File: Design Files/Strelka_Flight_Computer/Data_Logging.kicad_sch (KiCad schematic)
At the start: 2 parts

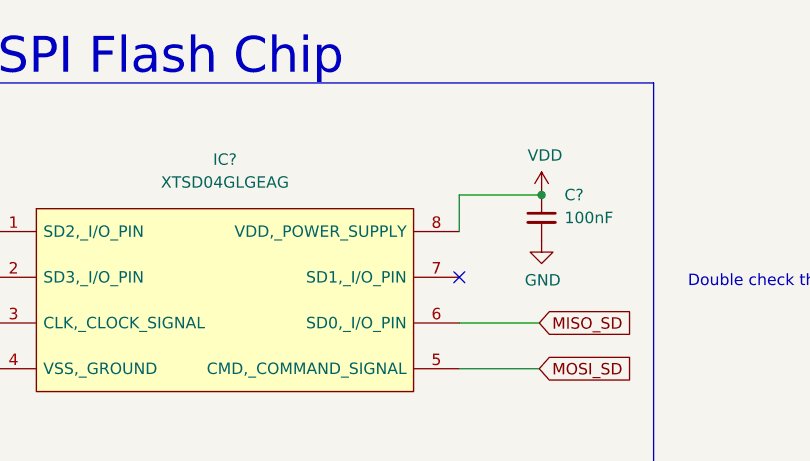
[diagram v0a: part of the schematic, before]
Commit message: Working SPICE sim for ematch continuity circuit
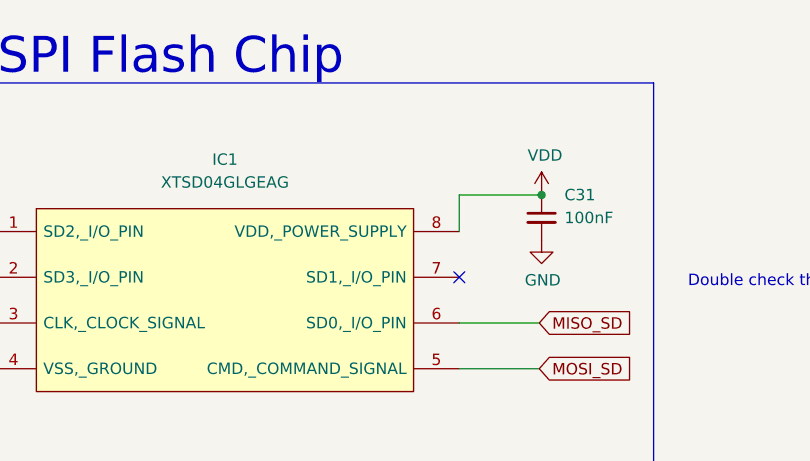
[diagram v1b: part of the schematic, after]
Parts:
- gave numbers to parts that had none: 2
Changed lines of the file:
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@@
   (symbol (lib_id "Device:C_Small") (at 106.299 41.656 0) (unit 1)
     (in_bom yes) (on_board yes)
-    (property "Reference" "C?" (id 0) (at 108.839 39.116 0)
+    (property "Reference" "C31" (id 0) (at 108.839 39.116 0)
       (effects (font (size 1.27 1.27)) (justify left))
     )
@@
   (symbol (lib_id "XTSD04GLGEAG:XTSD04GLGEAG") (at 45.085 50.8 0) (unit 1)
     (in_bom yes) (on_board yes) (fields_autoplaced)
-    (property "Reference" "IC?" (id 0) (at 71.12 35.179 0))
+    (property "Reference" "IC1" (id 0) (at 71.12 35.179 0))
     (property "Value" "XTSD04GLGEAG" (id 1) (at 71.12 37.719 0))
     (property "Footprint" "SON127P800X600X95-8N" (id 2) (at 104.775 48.26 0)
@@
   (symbol (lib_id "power:VDD") (at 106.299 39.116 0) (unit 1)
     (in_bom yes) (on_board yes)
-    (property "Reference" "#PWR?" (id 0) (at 106.299 42.926 0)
+    (property "Reference" "#PWR0194" (id 0) (at 106.299 42.926 0)
       (effects (font (size 1.27 1.27)) hide)
     )
@@
   (symbol (lib_id "power:GND") (at 106.299 44.196 0) (unit 1)
     (in_bom yes) (on_board yes)
-    (property "Reference" "#PWR?" (id 0) (at 106.299 50.546 0)
+    (property "Reference" "#PWR0195" (id 0) (at 106.299 50.546 0)
       (effects (font (size 1.27 1.27)) hide)
     )
@@
   (symbol (lib_id "power:GND") (at 41.275 60.96 0) (unit 1)
     (in_bom yes) (on_board yes)
-    (property "Reference" "#PWR?" (id 0) (at 41.275 67.31 0)
+    (property "Reference" "#PWR0196" (id 0) (at 41.275 67.31 0)
       (effects (font (size 1.27 1.27)) hide)
     )

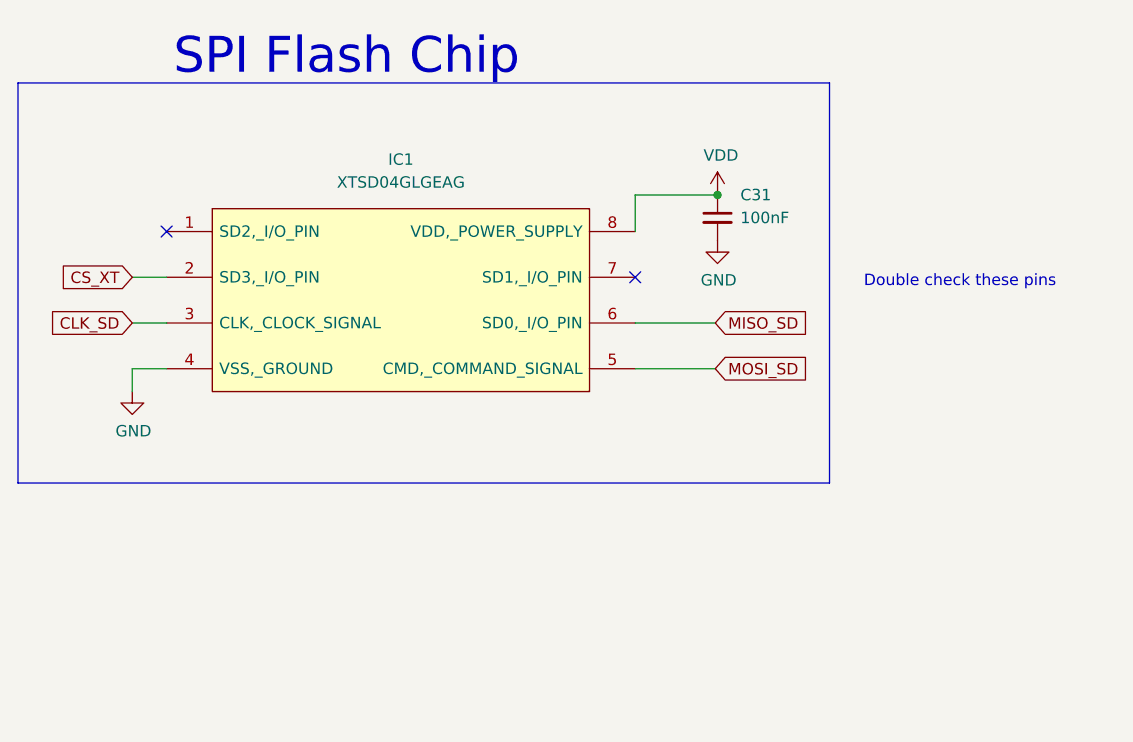
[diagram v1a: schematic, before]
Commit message: Added power board, almost finished Strelka schematic
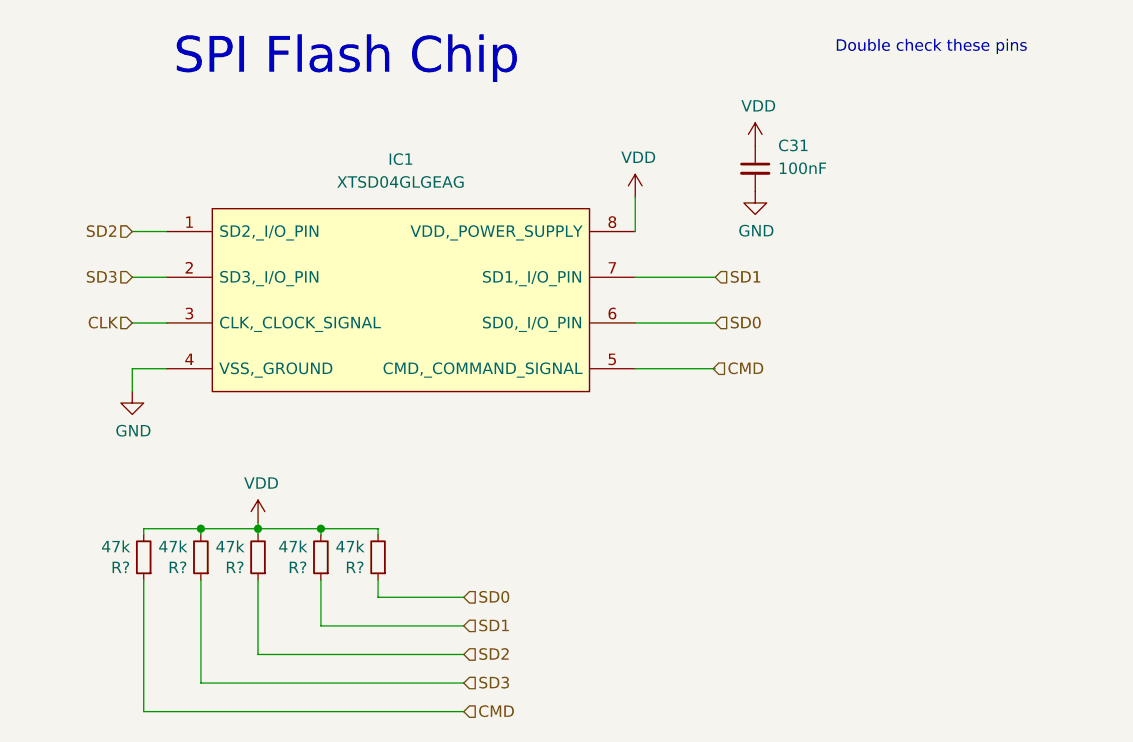
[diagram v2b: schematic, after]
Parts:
- added R? (x5): 47k, Resistor_SMD:R_0603_1608Metric_Pad0.98x0.95mm_HandSolder, symbol Nebula-rescue:R_Small-Device-H7_FlightComputer-rescue
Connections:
- net VDD: now also R?.2, R?.2, R?.2, R?.2, R?.2
- net SD2: now reaches IC1.1 (SD2,_I/O_PIN)
- net SD2: now also R?.1
- net SD1: now reaches IC1.7 (SD1,_I/O_PIN)
- net SD1: now also R?.1
- net CLK_SD renamed CLK
- net CS_XT renamed SD3
- net SD3: now also R?.1
- net MISO_SD renamed SD0
- net SD0: now also R?.1
- net MOSI_SD renamed CMD
- net CMD: now also R?.1
- no-connect marks 2 -> 0
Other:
- moved on the sheet: C31

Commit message: Added new UBLOX GPS
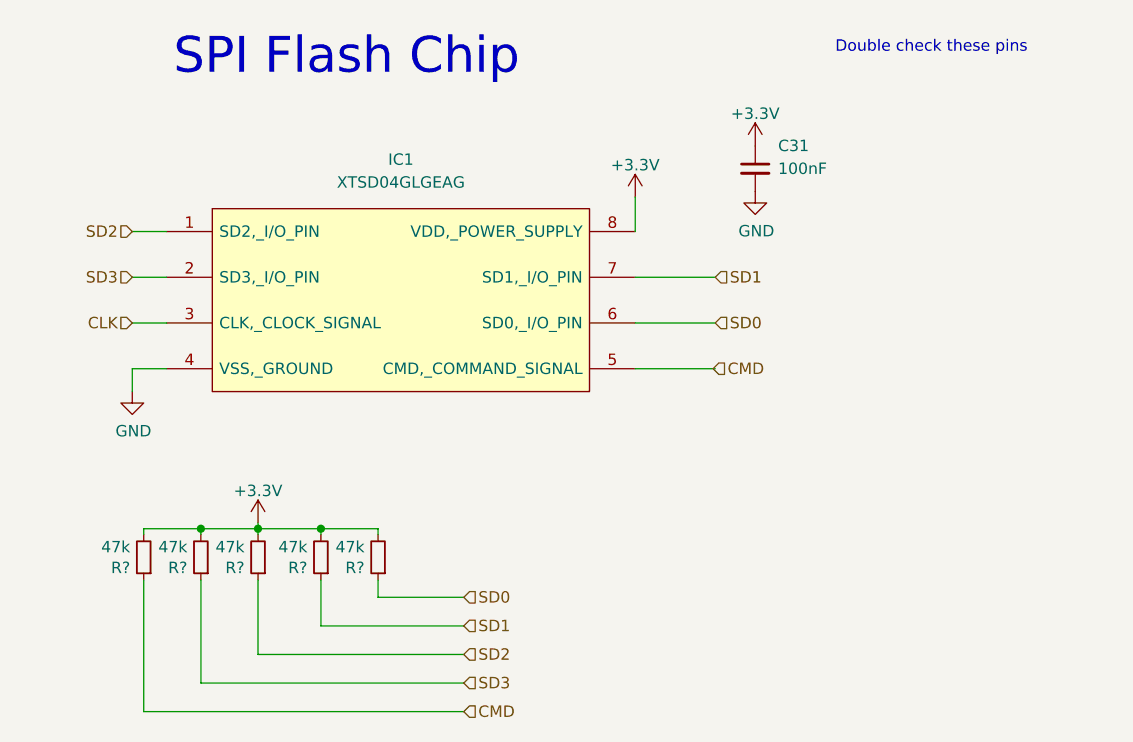
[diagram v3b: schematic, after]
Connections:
- net VDD renamed +3V3
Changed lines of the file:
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@@
     (pin "2")
   )
-  (symbol (lib_id "power:VDD") (at 97.155 39.37 0) (unit 1)
-    (in_bom yes) (on_board yes)
-    (property "Reference" "#PWR?" (id 0) (at 97.155 43.18 0)
+  (symbol (lib_id "power:+3.3V") (at 110.49 33.655 0) (unit 1)
+    (in_bom yes) (on_board yes) (fields_autoplaced)
+    (property "Reference" "#PWR?" (id 0) (at 110.49 37.465 0)
       (effects (font (size 1.27 1.27)) hide)
     )
-    (property "Value" "VDD" (id 1) (at 97.536 34.9758 0))
-    (property "Footprint" "" (id 2) (at 97.155 39.37 0)
+    (property "Value" "+3.3V" (id 1) (at 110.49 30.0792 0))
+    (property "Footprint" "" (id 2) (at 110.49 33.655 0)
       (effects (font (size 1.27 1.27)) hide)
     )
-    (property "Datasheet" "" (id 3) (at 97.155 39.37 0)
-      (effects (font (size 1.27 1.27)) hide)
-    )
-    (pin "1")
-  )
-  (symbol (lib_id "power:VDD") (at 55.245 75.565 0) (unit 1)
-    (in_bom yes) (on_board yes)
-    (property "Reference" "#PWR?" (id 0) (at 55.245 79.375 0)
-      (effects (font (size 1.27 1.27)) hide)
-    )
-    (property "Value" "VDD" (id 1) (at 55.626 71.1708 0))
-    (property "Footprint" "" (id 2) (at 55.245 75.565 0)
-      (effects (font (size 1.27 1.27)) hide)
-    )
-    (property "Datasheet" "" (id 3) (at 55.245 75.565 0)
+    (property "Datasheet" "" (id 3) (at 110.49 33.655 0)
       (effects (font (size 1.27 1.27)) hide)
     )
@@
     (pin "8")
   )
-  (symbol (lib_id "power:VDD") (at 110.49 33.655 0) (unit 1)
-    (in_bom yes) (on_board yes)
-    (property "Reference" "#PWR0194" (id 0) (at 110.49 37.465 0)
+  (symbol (lib_id "power:+3.3V") (at 97.155 39.37 0) (unit 1)
+    (in_bom yes) (on_board yes) (fields_autoplaced)
+    (property "Reference" "#PWR?" (id 0) (at 97.155 43.18 0)
       (effects (font (size 1.27 1.27)) hide)
     )
-    (property "Value" "VDD" (id 1) (at 110.871 29.2608 0))
-    (property "Footprint" "" (id 2) (at 110.49 33.655 0)
+    (property "Value" "+3.3V" (id 1) (at 97.155 35.7942 0))
+    (property "Footprint" "" (id 2) (at 97.155 39.37 0)
       (effects (font (size 1.27 1.27)) hide)
     )
-    (property "Datasheet" "" (id 3) (at 110.49 33.655 0)
+    (property "Datasheet" "" (id 3) (at 97.155 39.37 0)
       (effects (font (size 1.27 1.27)) hide)
     )
@@
       (effects (font (size 1.27 1.27)) hide)
     )
+    (pin "1")
+  )
+  (symbol (lib_id "power:+3.3V") (at 55.245 75.565 0) (unit 1)
+    (in_bom yes) (on_board yes) (fields_autoplaced)
+    (property "Reference" "#PWR?" (id 0) (at 55.245 79.375 0)
+      (effects (font (size 1.27 1.27)) hide)
+    )
+    (property "Value" "+3.3V" (id 1) (at 55.245 71.9892 0))
+    (property "Footprint" "" (id 2) (at 55.245 75.565 0)
+      (effects (font (size 1.27 1.27)) hide)
+    )
+    (property "Datasheet" "" (id 3) (at 55.245 75.565 0)
+      (effects (font (size 1.27 1.27)) hide)
+    )

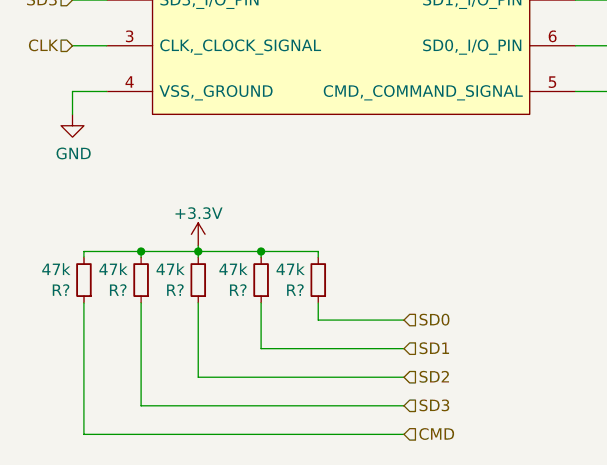
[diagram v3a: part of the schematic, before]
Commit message: Added motor driver to power board
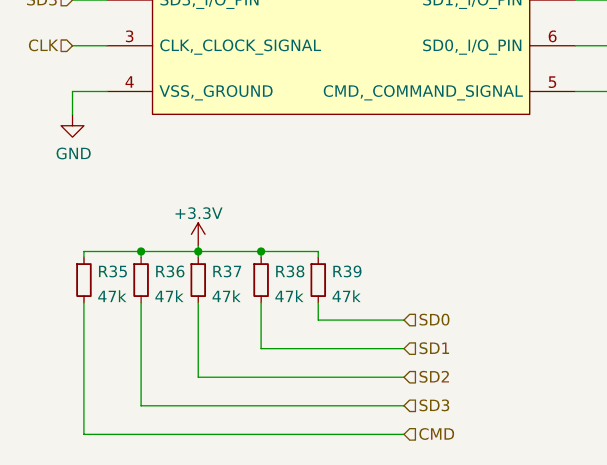
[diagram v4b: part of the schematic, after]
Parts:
- removed R? (x5): 47k, Resistor_SMD:R_0603_1608Metric_Pad0.98x0.95mm_HandSolder, symbol Nebula-rescue:R_Small-Device-H7_FlightComputer-rescue
- added R35, R36, R37, R38, R39: 47k, Resistor_SMD:R_0603_1608Metric, symbol Device:R_Small
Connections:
- net +3V3: now also R35.1, R36.1, R37.1, R38.1, R39.1
- net CMD: now also R35.2
- net SD0: now also R39.2
- net SD1: now also R38.2
- net SD2: now also R37.2
- net SD3: now also R36.2
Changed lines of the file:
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@@
     (effects (font (size 1.27 1.27)) (justify right))
   )
-  (symbol (lib_id "Nebula-rescue:R_Small-Device-H7_FlightComputer-rescue") (at 62.23 79.375 180) (unit 1)
-    (in_bom yes) (on_board yes)
-    (property "Reference" "R?" (id 0) (at 60.7314 80.5434 0)
-      (effects (font (size 1.27 1.27)) (justify left))
-    )
-    (property "Value" "47k" (id 1) (at 60.7314 78.232 0)
-      (effects (font (size 1.27 1.27)) (justify left))
-    )
-    (property "Footprint" "Resistor_SMD:R_0603_1608Metric_Pad0.98x0.95mm_HandSolder" (id 2) (at 62.23 79.375 0)
-      (effects (font (size 1.27 1.27)) hide)
-    )
-    (property "Datasheet" "~" (id 3) (at 62.23 79.375 0)
-      (effects (font (size 1.27 1.27)) hide)
-    )
-    (pin "1")
-    (pin "2")
-  )
   (symbol (lib_id "power:+3.3V") (at 110.49 33.655 0) (unit 1)
     (in_bom yes) (on_board yes) (fields_autoplaced)
-    (property "Reference" "#PWR?" (id 0) (at 110.49 37.465 0)
+    (property "Reference" "#PWR0171" (id 0) (at 110.49 37.465 0)
       (effects (font (size 1.27 1.27)) hide)
     )
@@
     )
     (pin "1")
+  )
+  (symbol (lib_id "Device:R_Small") (at 62.23 79.375 0) (unit 1)
+    (in_bom yes) (on_board yes) (fields_autoplaced)
+    (property "Reference" "R38" (id 0) (at 63.7287 78.4665 0)
+      (effects (font (size 1.27 1.27)) (justify left))
+    )
+    (property "Value" "47k" (id 1) (at 63.7287 81.2416 0)
+      (effects (font (size 1.27 1.27)) (justify left))
+    )
+    (property "Footprint" "Resistor_SMD:R_0603_1608Metric" (id 2) (at 62.23 79.375 0)
+      (effects (font (size 1.27 1.27)) hide)
+    )
+    (property "Datasheet" "~" (id 3) (at 62.23 79.375 0)
+      (effects (font (size 1.27 1.27)) hide)
+    )
+    (pin "1")
+    (pin "2")
   )
   (symbol (lib_id "Device:C_Small") (at 110.49 36.195 0) (unit 1)
@@
     (pin "8")
   )
+  (symbol (lib_id "Device:R_Small") (at 42.545 79.375 0) (unit 1)
+    (in_bom yes) (on_board yes) (fields_autoplaced)
+    (property "Reference" "R35" (id 0) (at 44.0437 78.4665 0)
+      (effects (font (size 1.27 1.27)) (justify left))
+    )
+    (property "Value" "47k" (id 1) (at 44.0437 81.2416 0)
+      (effects (font (size 1.27 1.27)) (justify left))
+    )
+    (property "Footprint" "Resistor_SMD:R_0603_1608Metric" (id 2) (at 42.545 79.375 0)
+      (effects (font (size 1.27 1.27)) hide)
+    )
+    (property "Datasheet" "~" (id 3) (at 42.545 79.375 0)
+      (effects (font (size 1.27 1.27)) hide)
+    )
+    (pin "1")
+    (pin "2")
+  )
   (symbol (lib_id "power:+3.3V") (at 97.155 39.37 0) (unit 1)
     (in_bom yes) (on_board yes) (fields_autoplaced)
-    (property "Reference" "#PWR?" (id 0) (at 97.155 43.18 0)
+    (property "Reference" "#PWR0170" (id 0) (at 97.155 43.18 0)
       (effects (font (size 1.27 1.27)) hide)
     )
@@
     (pin "1")
   )
-  (symbol (lib_id "Nebula-rescue:R_Small-Device-H7_FlightComputer-rescue") (at 55.245 79.375 180) (unit 1)
-    (in_bom yes) (on_board yes)
-    (property "Reference" "R?" (id 0) (at 53.7464 80.5434 0)
-      (effects (font (size 1.27 1.27)) (justify left))
-    )
-    (property "Value" "47k" (id 1) (at 53.7464 78.232 0)
-      (effects (font (size 1.27 1.27)) (justify left))
-    )
-    (property "Footprint" "Resistor_SMD:R_0603_1608Metric_Pad0.98x0.95mm_HandSolder" (id 2) (at 55.245 79.375 0)
+  (symbol (lib_id "Device:R_Small") (at 55.245 79.375 0) (unit 1)
+    (in_bom yes) (on_board yes) (fields_autoplaced)
+    (property "Reference" "R37" (id 0) (at 56.7437 78.4665 0)
+      (effects (font (size 1.27 1.27)) (justify left))
+    )
+    (property "Value" "47k" (id 1) (at 56.7437 81.2416 0)
+      (effects (font (size 1.27 1.27)) (justify left))
+    )
+    (property "Footprint" "Resistor_SMD:R_0603_1608Metric" (id 2) (at 55.245 79.375 0)
       (effects (font (size 1.27 1.27)) hide)
     )
@@
     (pin "2")
   )
-  (symbol (lib_id "Nebula-rescue:R_Small-Device-H7_FlightComputer-rescue") (at 48.895 79.375 180) (unit 1)
-    (in_bom yes) (on_board yes)
-    (property "Reference" "R?" (id 0) (at 47.3964 80.5434 0)
-      (effects (font (size 1.27 1.27)) (justify left))
-    )
-    (property "Value" "47k" (id 1) (at 47.3964 78.232 0)
-      (effects (font (size 1.27 1.27)) (justify left))
-    )
-    (property "Footprint" "Resistor_SMD:R_0603_1608Metric_Pad0.98x0.95mm_HandSolder" (id 2) (at 48.895 79.375 0)
+  (symbol (lib_id "Device:R_Small") (at 48.895 79.375 0) (unit 1)
+    (in_bom yes) (on_board yes) (fields_autoplaced)
+    (property "Reference" "R36" (id 0) (at 50.3937 78.4665 0)
+      (effects (font (size 1.27 1.27)) (justify left))
+    )
+    (property "Value" "47k" (id 1) (at 50.3937 81.2416 0)
+      (effects (font (size 1.27 1.27)) (justify left))
+    )
+    (property "Footprint" "Resistor_SMD:R_0603_1608Metric" (id 2) (at 48.895 79.375 0)
       (effects (font (size 1.27 1.27)) hide)
     )
     (property "Datasheet" "~" (id 3) (at 48.895 79.375 0)
+      (effects (font (size 1.27 1.27)) hide)
+    )
+    (pin "1")
+    (pin "2")
+  )
+  (symbol (lib_id "Device:R_Small") (at 68.58 79.375 0) (unit 1)
+    (in_bom yes) (on_board yes) (fields_autoplaced)
+    (property "Reference" "R39" (id 0) (at 70.0787 78.4665 0)
+      (effects (font (size 1.27 1.27)) (justify left))
+    )
+    (property "Value" "47k" (id 1) (at 70.0787 81.2416 0)
+      (effects (font (size 1.27 1.27)) (justify left))
+    )
+    (property "Footprint" "Resistor_SMD:R_0603_1608Metric" (id 2) (at 68.58 79.375 0)
+      (effects (font (size 1.27 1.27)) hide)
+    )
+    (property "Datasheet" "~" (id 3) (at 68.58 79.375 0)
       (effects (font (size 1.27 1.27)) hide)
     )
@@
     (pin "1")
   )
-  (symbol (lib_id "Nebula-rescue:R_Small-Device-H7_FlightComputer-rescue") (at 68.58 79.375 180) (unit 1)
-    (in_bom yes) (on_board yes)
-    (property "Reference" "R?" (id 0) (at 67.0814 80.5434 0)
-      (effects (font (size 1.27 1.27)) (justify left))
-    )
-    (property "Value" "47k" (id 1) (at 67.0814 78.232 0)
-      (effects (font (size 1.27 1.27)) (justify left))
-    )
-    (property "Footprint" "Resistor_SMD:R_0603_1608Metric_Pad0.98x0.95mm_HandSolder" (id 2) (at 68.58 79.375 0)
-      (effects (font (size 1.27 1.27)) hide)
-    )
-    (property "Datasheet" "~" (id 3) (at 68.58 79.375 0)
-      (effects (font (size 1.27 1.27)) hide)
-    )
-    (pin "1")
-    (pin "2")
-  )
-  (symbol (lib_id "Nebula-rescue:R_Small-Device-H7_FlightComputer-rescue") (at 42.545 79.375 180) (unit 1)
-    (in_bom yes) (on_board yes)
-    (property "Reference" "R?" (id 0) (at 41.0464 80.5434 0)
-      (effects (font (size 1.27 1.27)) (justify left))
-    )
-    (property "Value" "47k" (id 1) (at 41.0464 78.232 0)
-      (effects (font (size 1.27 1.27)) (justify left))
-    )
-    (property "Footprint" "Resistor_SMD:R_0603_1608Metric_Pad0.98x0.95mm_HandSolder" (id 2) (at 42.545 79.375 0)
-      (effects (font (size 1.27 1.27)) hide)
-    )
-    (property "Datasheet" "~" (id 3) (at 42.545 79.375 0)
-      (effects (font (size 1.27 1.27)) hide)
-    )
-    (pin "1")
-    (pin "2")
-  )
   (symbol (lib_id "power:GND") (at 41.275 60.96 0) (unit 1)
     (in_bom yes) (on_board yes)
@@
   (symbol (lib_id "power:+3.3V") (at 55.245 75.565 0) (unit 1)
     (in_bom yes) (on_board yes) (fields_autoplaced)
-    (property "Reference" "#PWR?" (id 0) (at 55.245 79.375 0)
-      (effects (font (size 1.27 1.27)) hide)
-    )
+    (property "Reference" "#PWR0169" (id 0) (at 55.245 79.375 0)
+      (effects (font (size 1.27 1.27)) hide)
+    )

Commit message: Creating BOM
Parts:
- IC1: Height 0.95 -> (none); LCSC# (none) -> C558839; Manufacturer_Name XTX -> (none); Manufacturer_Part_Number XTSD04GLGEAG -> (none)
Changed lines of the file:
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@@
       (effects (font (size 1.27 1.27)) (justify left) hide)
     )
-    (property "Description" "LGA8-8x6mm FLASH" (id 4) (at 104.775 53.34 0)
-      (effects (font (size 1.27 1.27)) (justify left) hide)
-    )
-    (property "Height" "0.95" (id 5) (at 104.775 55.88 0)
-      (effects (font (size 1.27 1.27)) (justify left) hide)
-    )
-    (property "Manufacturer_Name" "XTX" (id 6) (at 104.775 58.42 0)
-      (effects (font (size 1.27 1.27)) (justify left) hide)
-    )
-    (property "Manufacturer_Part_Number" "XTSD04GLGEAG" (id 7) (at 104.775 60.96 0)
-      (effects (font (size 1.27 1.27)) (justify left) hide)
-    )
-    (property "Mouser Part Number" "" (id 8) (at 104.775 63.5 0)
-      (effects (font (size 1.27 1.27)) (justify left) hide)
-    )
-    (property "Mouser Price/Stock" "" (id 9) (at 104.775 66.04 0)
-      (effects (font (size 1.27 1.27)) (justify left) hide)
-    )
-    (property "Arrow Part Number" "" (id 10) (at 104.775 68.58 0)
-      (effects (font (size 1.27 1.27)) (justify left) hide)
-    )
-    (property "Arrow Price/Stock" "" (id 11) (at 104.775 71.12 0)
-      (effects (font (size 1.27 1.27)) (justify left) hide)
+    (property "LCSC#" "C558839" (id 4) (at 45.085 50.8 0)
+      (effects (font (size 1.27 1.27)) hide)
     )
     (pin "1")

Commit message: redo placement
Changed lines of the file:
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@@
     (effects (font (size 1.27 1.27)) (justify right))
   )
-  (hierarchical_label "CMD" (shape input) (at 105.8054 58.42 0)
+  (hierarchical_label "CMD" (shape input) (at 106.045 58.42 0)
     (effects (font (size 1.27 1.27)) (justify left))
   )
